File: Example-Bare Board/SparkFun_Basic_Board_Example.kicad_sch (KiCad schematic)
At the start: 20 parts, among them J1 Qwiic_RA, U2 RT9080-3.3

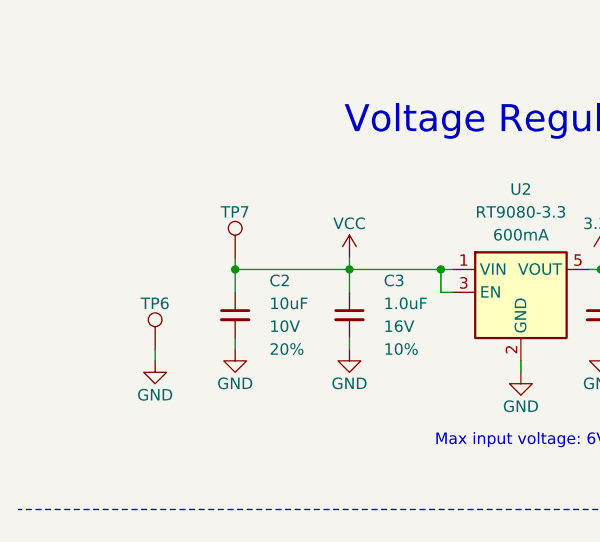
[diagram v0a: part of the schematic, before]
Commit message: Update examples to KiCad v9
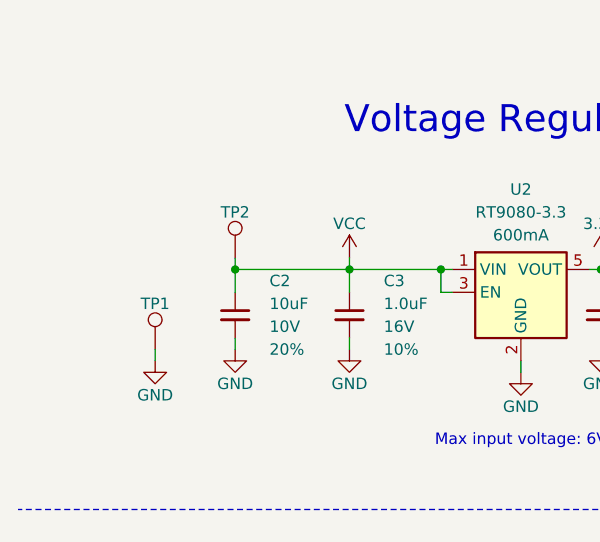
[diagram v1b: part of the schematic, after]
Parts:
- renumbered TP6 to TP1, TP7 to TP2
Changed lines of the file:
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@@
 (kicad_sch
-	(version 20231120)
+	(version 20250114)
 	(generator "eeschema")
-	(generator_version "8.0")
+	(generator_version "9.0")
 	(paper "USLetter")
 	(title_block
@@
 		(comment 1 "Designed by: You")
 	)
+	(text "Voltage Regulation"
+		(exclude_from_sim no)
+		(at 68.58 24.13 0)
+		(effects
+			(font
+				(size 3 3)
+			)
+		)
+	)
+	(text "Qwiic Connector"
+		(exclude_from_sim no)
+		(at 64.77 78.74 0)
+		(effects
+			(font
+				(size 3 3)
+			)
+		)
+	)
+	(text "Max input voltage: 6V"
+		(exclude_from_sim no)
+		(at 68.58 59.69 0)
+		(effects
+			(font
+				(size 1.27 1.27)
+			)
+		)
+	)
 	(junction
 		(at 49.53 40.64)
@@
 		)
 	)
-	(text "Voltage Regulation"
-		(exclude_from_sim no)
-		(at 68.58 24.13 0)
-		(effects
-			(font
-				(size 3 3)
-			)
-		)
-	)
-	(text "Qwiic Connector"
-		(exclude_from_sim no)
-		(at 64.77 78.74 0)
-		(effects
-			(font
-				(size 3 3)
-			)
-		)
-	)
-	(text "Max input voltage: 6V"
-		(exclude_from_sim no)
-		(at 68.58 59.69 0)
+	(global_label "SCL"
+		(shape input)
+		(at 57.15 96.52 180)
+		(fields_autoplaced yes)
 		(effects
 			(font
 				(size 1.27 1.27)
 			)
-		)
-	)
-	(global_label "SCL"
+			(justify right)
+		)
+		(property "Intersheetrefs" "${INTERSHEET_REFS}"
+			(at 50.6572 96.52 0)
+			(effects
+				(font
+					(size 1.27 1.27)
+				)
+				(justify right)
+				(hide yes)
+			)
+		)
+	)
+	(global_label "SDA"
 		(shape input)
-		(at 57.15 96.52 180)
+		(at 57.15 99.06 180)
 		(fields_autoplaced yes)
 		(effects
@@
 		)
 		(property "Intersheetrefs" "${INTERSHEET_REFS}"
-			(at 50.6572 96.52 0)
-			(effects
-				(font
-					(size 1.27 1.27)
-				)
-				(justify right)
-				(hide yes)
-			)
-		)
-	)
-	(global_label "SDA"
-		(shape input)
-		(at 57.15 99.06 180)
-		(fields_autoplaced yes)
-		(effects
-			(font
-				(size 1.27 1.27)
-			)
-			(justify right)
-		)
-		(property "Intersheetrefs" "${INTERSHEET_REFS}"
 			(at 50.5967 99.06 0)
 			(effects
@@
 		(dnp no)
 		(fields_autoplaced yes)
-		(property "Reference" "TP6"
+		(property "Reference" "TP1"
 			(at 27.94 44.45 0)
 			(effects
@@
 		(dnp no)
 		(fields_autoplaced yes)
-		(property "Reference" "TP7"
+		(property "Reference" "TP2"
 			(at 36.83 34.29 0)
 			(effects
@@
 		)
 	)
+	(embedded_fonts no)
 )
